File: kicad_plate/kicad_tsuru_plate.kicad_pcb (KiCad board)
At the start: 2 copper layers, 209.6 x 57.1 mm, 0 parts

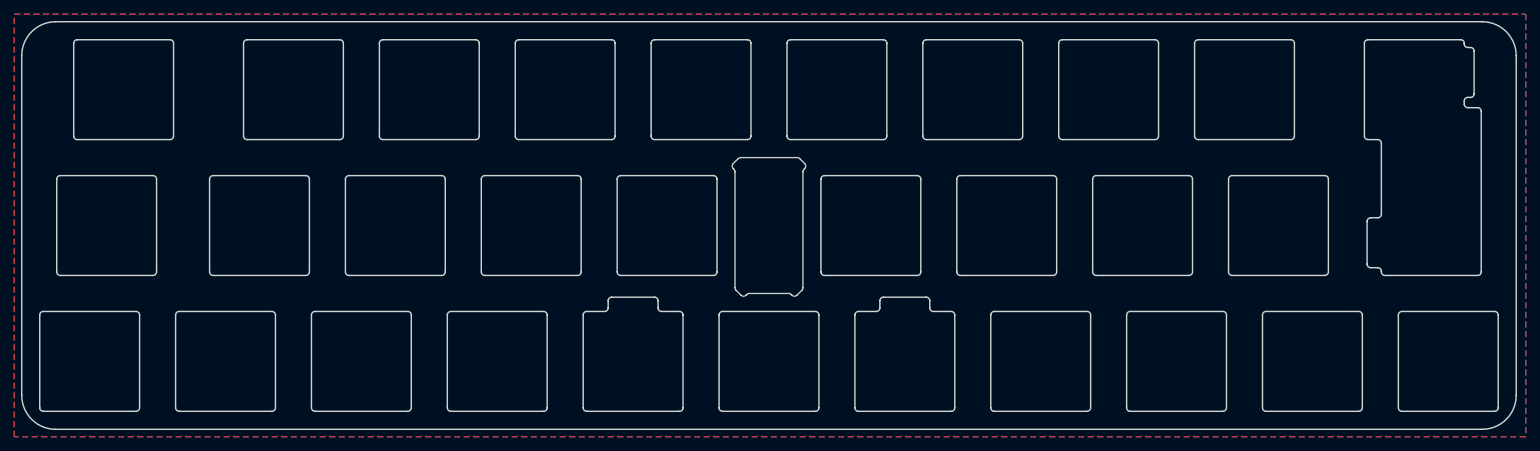
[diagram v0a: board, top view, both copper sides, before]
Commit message: add holes for reaching pcb screws
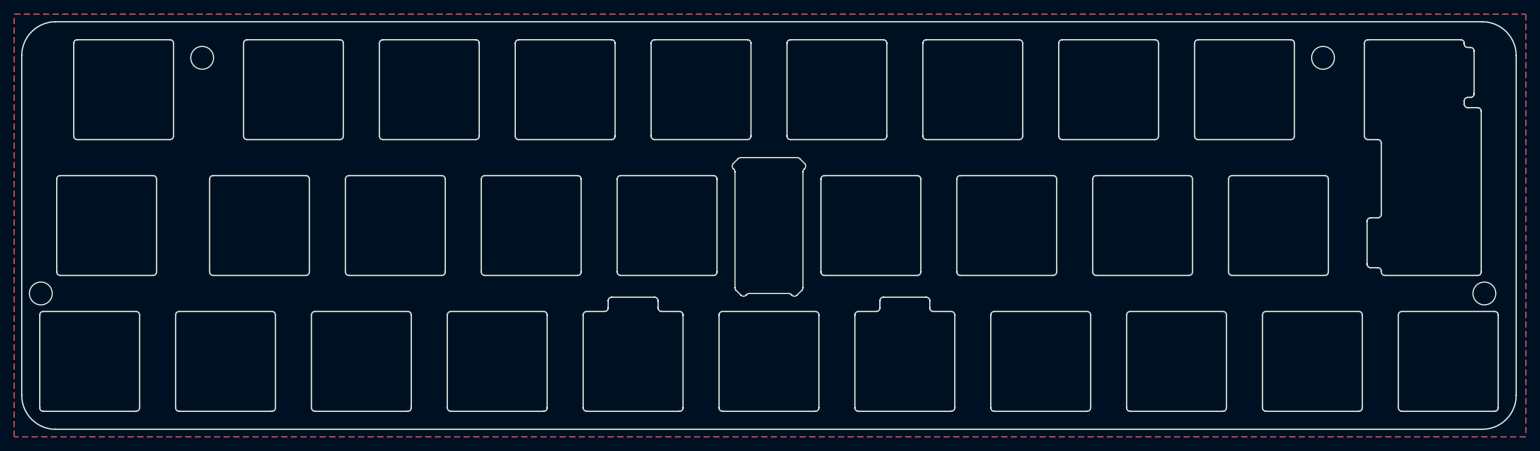
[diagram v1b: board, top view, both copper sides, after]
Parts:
- added H1: MountingHole, MountingHole:MountingHole_3.2mm_M3, F.Cu at (61.8, 70.5)
- added H2: MountingHole, MountingHole:MountingHole_3.2mm_M3, F.Cu at (218.9, 70.5)
- added H3: MountingHole, MountingHole:MountingHole_3.2mm_M3, F.Cu at (39.1, 103.6)
- added H4: MountingHole, MountingHole:MountingHole_3.2mm_M3, F.Cu at (241.6, 103.6)
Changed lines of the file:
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@@
   )
   (net 0 "")
+  (footprint "MountingHole:MountingHole_3.2mm_M3" (layer "F.Cu")
+    (at 39.147067 103.58516)
+    (descr "Mounting Hole 3.2mm, no annular, M3")
+    (tags "mounting hole 3.2mm no annular m3")
+    (property "Sheetfile" "kicad_tsuru_plate.kicad_sch")
+    (property "Sheetname" "")
+    (property "ki_description" "Mounting Hole without connection")
+    (property "ki_keywords" "mounting hole")
+    (attr exclude_from_pos_files)
+    (fp_text reference "H3" (at 0 -4.2) (layer "F.SilkS") hide
+        (effects (font (size 1 1) (thickness 0.15)))
+    )
+    (fp_text value "MountingHole" (at 0 4.2) (layer "F.Fab")
+        (effects (font (size 1 1) (thickness 0.15)))
+    )
+    (fp_text user "${REFERENCE}" (at 0 0) (layer "F.Fab")
+        (effects (font (size 1 1) (thickness 0.15)))
+    )
+    (fp_circle (center 0 0) (end 3.45 0)
+      (stroke (width 0.05) (type solid)) (fill none) (layer "F.CrtYd"))
+    (pad "" np_thru_hole circle (at 0 0) (size 3.2 3.2) (drill 3.2) (layers "*.Cu" "*.Mask"))
+  )
+  (footprint "MountingHole:MountingHole_3.2mm_M3" (layer "F.Cu")
+    (at 218.931963 70.54516)
+    (descr "Mounting Hole 3.2mm, no annular, M3")
+    (tags "mounting hole 3.2mm no annular m3")
+    (property "Sheetfile" "kicad_tsuru_plate.kicad_sch")
+    (property "Sheetname" "")
+    (property "ki_description" "Mounting Hole without connection")
+    (property "ki_keywords" "mounting hole")
+    (attr exclude_from_pos_files)
+    (fp_text reference "H2" (at 0 -4.2) (layer "F.SilkS") hide
+        (effects (font (size 1 1) (thickness 0.15)))
+    )
+    (fp_text value "MountingHole" (at 0 4.2) (layer "F.Fab")
+        (effects (font (size 1 1) (thickness 0.15)))
+    )
+    (fp_text user "${REFERENCE}" (at 0 0) (layer "F.Fab")
+        (effects (font (size 1 1) (thickness 0.15)))
+    )
+    (fp_circle (center 0 0) (end 3.45 0)
+      (stroke (width 0.05) (type solid)) (fill none) (layer "F.CrtYd"))
+    (pad "" np_thru_hole circle (at 0 0) (size 3.2 3.2) (drill 3.2) (layers "*.Cu" "*.Mask"))
+  )
+  (footprint "MountingHole:MountingHole_3.2mm_M3" (layer "F.Cu")
+    (at 241.553895 103.585087)
+    (descr "Mounting Hole 3.2mm, no annular, M3")
+    (tags "mounting hole 3.2mm no annular m3")
+    (property "Sheetfile" "kicad_tsuru_plate.kicad_sch")
+    (property "Sheetname" "")
+    (property "ki_description" "Mounting Hole without connection")
+    (property "ki_keywords" "mounting hole")
+    (attr exclude_from_pos_files)
+    (fp_text reference "H4" (at 0 -4.2) (layer "F.SilkS") hide
+        (effects (font (size 1 1) (thickness 0.15)))
+    )
+    (fp_text value "MountingHole" (at 0 4.2) (layer "F.Fab")
+        (effects (font (size 1 1) (thickness 0.15)))
+    )
+    (fp_text user "${REFERENCE}" (at 0 0) (layer "F.Fab")
+        (effects (font (size 1 1) (thickness 0.15)))
+    )
+    (fp_circle (center 0 0) (end 3.45 0)
+      (stroke (width 0.05) (type solid)) (fill none) (layer "F.CrtYd"))
+    (pad "" np_thru_hole circle (at 0 0) (size 3.2 3.2) (drill 3.2) (layers "*.Cu" "*.Mask"))
+  )
+  (footprint "MountingHole:MountingHole_3.2mm_M3" (layer "F.Cu")
+    (at 61.769067 70.54516)
+    (descr "Mounting Hole 3.2mm, no annular, M3")
+    (tags "mounting hole 3.2mm no annular m3")
+    (property "Sheetfile" "kicad_tsuru_plate.kicad_sch")
+    (property "Sheetname" "")
+    (property "ki_description" "Mounting Hole without connection")
+    (property "ki_keywords" "mounting hole")
+    (attr exclude_from_pos_files)
+    (fp_text reference "H1" (at 0 -4.2) (layer "F.SilkS") hide
+        (effects (font (size 1 1) (thickness 0.15)))
+    )
+    (fp_text value "MountingHole" (at 0 4.2) (layer "F.Fab")
+        (effects (font (size 1 1) (thickness 0.15)))
+    )
+    (fp_text user "${REFERENCE}" (at 0 0) (layer "F.Fab")
+        (effects (font (size 1 1) (thickness 0.15)))
+    )
+    (fp_circle (center 0 0) (end 3.45 0)
+      (stroke (width 0.05) (type solid)) (fill none) (layer "F.CrtYd"))
+    (pad "" np_thru_hole circle (at 0 0) (size 3.2 3.2) (drill 3.2) (layers "*.Cu" "*.Mask"))
+  )
   (gr_arc (start 68.068067 82.00966) (mid 67.714494 81.863228) (end 67.568067 81.50966)
     (stroke (width 0.2) (type solid)) (layer "Edge.Cuts"))

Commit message: fix plate file
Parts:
- moved H2 0.89 mm to (219.8, 70.5)
- moved H1 0.89 mm to (62.7, 70.5)
- moved H3 0.89 mm to (40.0, 103.6)
- moved H4 0.89 mm to (242.4, 103.6)
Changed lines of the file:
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@@
   (net 0 "")
   (footprint "MountingHole:MountingHole_3.2mm_M3" (layer "F.Cu")
-    (at 39.147067 103.58516)
+    (at 40.039567 103.58516)
     (descr "Mounting Hole 3.2mm, no annular, M3")
     (tags "mounting hole 3.2mm no annular m3")
@@
   )
   (footprint "MountingHole:MountingHole_3.2mm_M3" (layer "F.Cu")
-    (at 218.931963 70.54516)
+    (at 219.824463 70.54516)
     (descr "Mounting Hole 3.2mm, no annular, M3")
     (tags "mounting hole 3.2mm no annular m3")
@@
   )
   (footprint "MountingHole:MountingHole_3.2mm_M3" (layer "F.Cu")
-    (at 241.553895 103.585087)
+    (at 242.446395 103.585087)
     (descr "Mounting Hole 3.2mm, no annular, M3")
     (tags "mounting hole 3.2mm no annular m3")
@@
   )
   (footprint "MountingHole:MountingHole_3.2mm_M3" (layer "F.Cu")
-    (at 61.769067 70.54516)
+    (at 62.661567 70.54516)
     (descr "Mounting Hole 3.2mm, no annular, M3")
     (tags "mounting hole 3.2mm no annular m3")
